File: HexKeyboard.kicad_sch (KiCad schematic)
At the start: 82 parts, among them J1 Conn_02x04_Odd_Even, J2 Conn_01x04, J4 USB_A, J9 Micro_SD_Card, SW1 SW_1, SW10 SW_10, SW11 SW_11, SW12 SW_12, SW13 SW_13, SW14 SW_14, SW15 SW_15, SW16 SW_16, SW17 SW_17, SW18 SW_18, SW19 SW_19, SW2 SW_2, SW20 SW_20, SW21 SW_21, SW22 SW_22, SW23 SW_23, SW24 SW_24, SW25 SW_25, SW3 SW_3, SW4 SW_4, SW5 SW_5, SW6 SW_6, SW7 SW_7, SW8 SW_8, SW9 SW_9, U1 ATmega32U4-AU, U2 AMS1117-3.3, U3 74LVC125, U4 AT24CS64-XHM, U5 MAX7219, Y1 16MHz

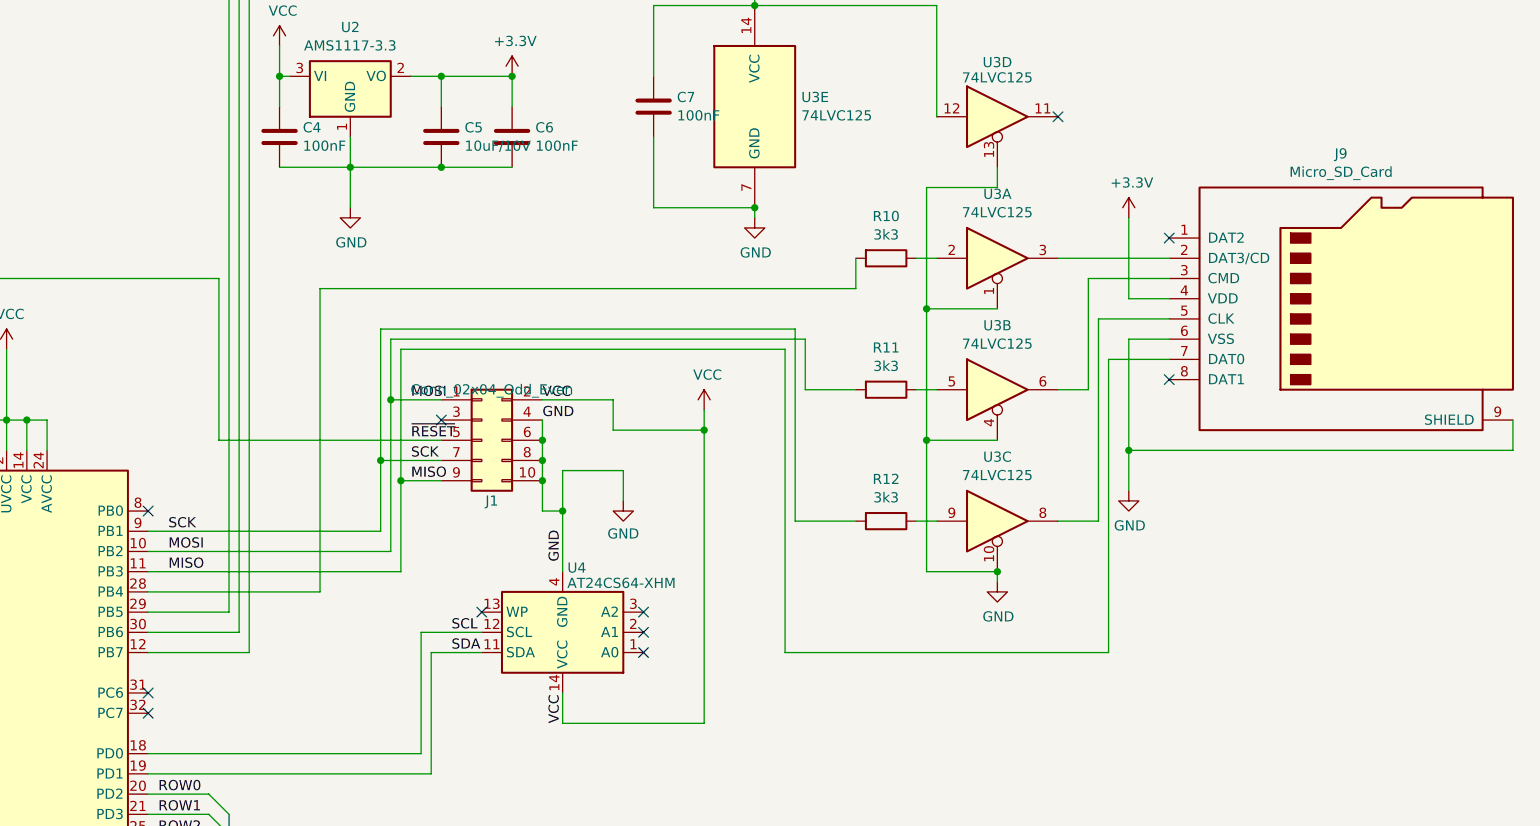
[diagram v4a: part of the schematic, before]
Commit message: Switched to the correct MicroSD holder
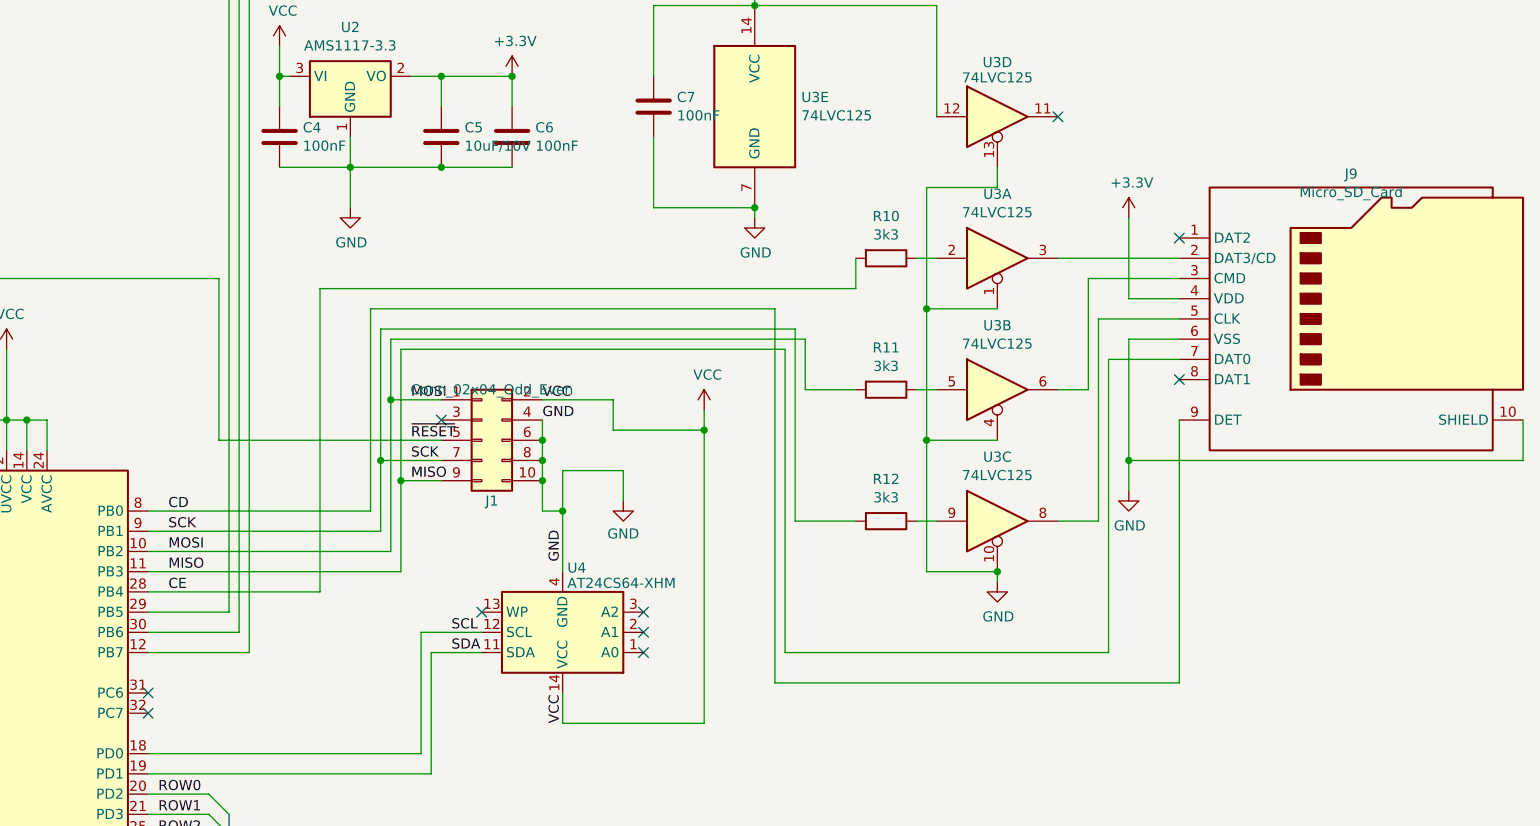
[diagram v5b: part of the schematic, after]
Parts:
- J9: footprint Connector_Card:microSD_HC_Wuerth_693072010801 -> MicroSD:GCT_MEM2075; symbol Connector:Micro_SD_Card -> Connector:Micro_SD_Card_Det1
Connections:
- net GND: now also J9.10 (SHIELD); no longer J9.9 (SHIELD)
- net CE: now reaches R10.2, U1.28 (PB4)
- net CD: now reaches U1.8 (PB0)
- net CD: now also J9.9 (DET)
- no-connect marks 18 -> 17
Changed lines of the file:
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@@
   (junction (at 96.52 83.82) (diameter 0) (color 0 0 0 0)
   )
-  (junction (at 312.42 151.13) (diameter 0) (color 0 0 0 0)
-  )
   (junction (at 171.45 147.32) (diameter 0) (color 0 0 0 0)
   )
@@
   )
   (junction (at 68.58 111.76) (diameter 0) (color 0 0 0 0)
+  )
+  (junction (at 312.42 152.4) (diameter 0) (color 0 0 0 0)
   )
   (junction (at 132.08 217.17) (diameter 0) (color 0 0 0 0)
@@
   (no_connect (at 251.46 176.53))
   (no_connect (at 251.46 171.45))
-  (no_connect (at 189.23 158.75))
-  (no_connect (at 317.5 124.46))
+  (no_connect (at 318.77 124.46))
   (no_connect (at 189.23 214.63))
   (no_connect (at 251.46 173.99))
@@
   (no_connect (at 226.06 147.32))
   (no_connect (at 189.23 207.01))
-  (no_connect (at 317.5 142.24))
+  (no_connect (at 318.77 142.24))
   (no_connect (at 231.14 171.45))
   (no_connect (at 189.23 212.09))
@@
     (stroke (width 0) (type default))
   )
-  (wire (pts (xy 308.61 134.62) (xy 317.5 134.62))
+  (wire (pts (xy 308.61 134.62) (xy 318.77 134.62))
     (stroke (width 0) (type default))
   )
@@
     (stroke (width 0) (type default))
   )
-  (wire (pts (xy 312.42 137.16) (xy 312.42 151.13))
-    (stroke (width 0) (type default))
-  )
   (wire (pts (xy 189.23 196.85) (xy 196.85 196.85))
     (stroke (width 0) (type default))
@@
     (stroke (width 0) (type default))
   )
+  (wire (pts (xy 312.42 152.4) (xy 312.42 156.21))
+    (stroke (width 0) (type default))
+  )
   (wire (pts (xy 252.73 104.14) (xy 252.73 95.25))
     (stroke (width 0) (type default))
@@
     (stroke (width 0) (type default))
   )
+  (wire (pts (xy 267.97 133.35) (xy 217.17 133.35))
+    (stroke (width 0) (type default))
+  )
   (wire (pts (xy 50.8 96.52) (xy 50.8 111.76))
     (stroke (width 0) (type default))
@@
     (stroke (width 0) (type default))
   )
+  (wire (pts (xy 267.97 180.34) (xy 267.97 133.35))
+    (stroke (width 0) (type default))
+  )
   (wire (pts (xy 214.63 111.76) (xy 214.63 115.57))
     (stroke (width 0) (type default))
@@
     (stroke (width 0) (type default))
   )
+  (wire (pts (xy 217.17 158.75) (xy 189.23 158.75))
+    (stroke (width 0) (type default))
+  )
   (wire (pts (xy 121.92 111.76) (xy 121.92 115.57))
     (stroke (width 0) (type default))
   )
-  (wire (pts (xy 307.34 129.54) (xy 317.5 129.54))
-    (stroke (width 0) (type default))
-  )
-  (wire (pts (xy 309.88 139.7) (xy 317.5 139.7))
+  (wire (pts (xy 307.34 129.54) (xy 318.77 129.54))
+    (stroke (width 0) (type default))
+  )
+  (wire (pts (xy 309.88 139.7) (xy 318.77 139.7))
     (stroke (width 0) (type default))
   )
@@
     (stroke (width 0) (type default))
   )
-  (wire (pts (xy 303.53 127) (xy 317.5 127))
-    (stroke (width 0) (type default))
-  )
   (bus (pts (xy 199.39 224.79) (xy 199.39 227.33))
     (stroke (width 0) (type default))
@@
     (stroke (width 0) (type default))
   )
-  (wire (pts (xy 360.68 147.32) (xy 360.68 151.13))
+  (wire (pts (xy 361.95 147.32) (xy 361.95 152.4))
     (stroke (width 0) (type default))
   )
@@
     (stroke (width 0) (type default))
   )
-  (wire (pts (xy 317.5 137.16) (xy 312.42 137.16))
+  (wire (pts (xy 318.77 137.16) (xy 312.42 137.16))
     (stroke (width 0) (type default))
   )
@@
     (stroke (width 0) (type default))
   )
-  (wire (pts (xy 312.42 151.13) (xy 312.42 156.21))
-    (stroke (width 0) (type default))
-  )
   (wire (pts (xy 100.33 234.95) (xy 116.84 234.95))
     (stroke (width 0) (type default))
@@
     (stroke (width 0) (type default))
   )
+  (wire (pts (xy 217.17 133.35) (xy 217.17 158.75))
+    (stroke (width 0) (type default))
+  )
   (wire (pts (xy 114.3 99.06) (xy 132.08 99.06))
     (stroke (width 0) (type default))
@@
     (stroke (width 0) (type default))
   )
+  (wire (pts (xy 312.42 137.16) (xy 312.42 152.4))
+    (stroke (width 0) (type default))
+  )
   (wire (pts (xy 223.52 189.23) (xy 223.52 173.99))
     (stroke (width 0) (type default))
@@
     (stroke (width 0) (type default))
   )
+  (wire (pts (xy 318.77 180.34) (xy 267.97 180.34))
+    (stroke (width 0) (type default))
+  )
   (bus (pts (xy 176.53 52.07) (xy 176.53 58.42))
     (stroke (width 0) (type default))
@@
     (stroke (width 0) (type default))
   )
-  (wire (pts (xy 317.5 132.08) (xy 312.42 132.08))
+  (wire (pts (xy 318.77 147.32) (xy 318.77 180.34))
+    (stroke (width 0) (type default))
+  )
+  (wire (pts (xy 318.77 132.08) (xy 312.42 132.08))
     (stroke (width 0) (type default))
   )
@@
     (stroke (width 0) (type default))
   )
-  (wire (pts (xy 360.68 151.13) (xy 312.42 151.13))
+  (wire (pts (xy 361.95 152.4) (xy 312.42 152.4))
     (stroke (width 0) (type default))
   )
@@
     (stroke (width 0) (type default))
   )
+  (wire (pts (xy 303.53 127) (xy 318.77 127))
+    (stroke (width 0) (type default))
+  )
   (wire (pts (xy 60.96 52.07) (xy 60.96 49.53))
     (stroke (width 0) (type default))
@@
     (effects (font (size 1.27 1.27)) (justify left bottom))
   )
+  (label "CD" (at 191.77 158.75 0) (fields_autoplaced)
+    (effects (font (size 1.27 1.27)) (justify left bottom))
+  )
   (label "VCC" (at 241.3 185.42 90) (fields_autoplaced)
     (effects (font (size 1.27 1.27)) (justify left bottom))
@@
   )
   (label "SCK" (at 191.77 161.29 0) (fields_autoplaced)
+    (effects (font (size 1.27 1.27)) (justify left bottom))
+  )
+  (label "CE" (at 191.77 168.91 0) (fields_autoplaced)
     (effects (font (size 1.27 1.27)) (justify left bottom))
   )
@@
     )
   )
-  (symbol (lib_id "Connector:Micro_SD_Card") (at 340.36 132.08 0) (unit 1)
-    (in_bom yes) (on_board yes) (dnp no)
-    (property "Reference" "J9" (at 339.09 113.8682 0)
-      (effects (font (size 1.27 1.27)))
-    )
-    (property "Value" "Micro_SD_Card" (at 339.09 116.1796 0)
-      (effects (font (size 1.27 1.27)))
-    )
-    (property "Footprint" "Connector_Card:microSD_HC_Wuerth_693072010801" (at 369.57 124.46 0)
-      (effects (font (size 1.27 1.27)) hide)
-    )
-    (property "Datasheet" "http://katalog.we-online.de/em/datasheet/693072010801.pdf" (at 340.36 132.08 0)
-      (effects (font (size 1.27 1.27)) hide)
-    )
-    (property "LCSC" "C5912397" (at 340.36 132.08 0)
-      (effects (font (size 1.27 1.27)) hide)
-    )
-    (pin "1")
+  (symbol (lib_id "Connector:Micro_SD_Card_Det1") (at 341.63 134.62 0) (unit 1)
+    (in_bom yes) (on_board yes) (dnp no)
+    (property "Reference" "J9" (at 340.36 116.4082 0)
+      (effects (font (size 1.27 1.27)))
+    )
+    (property "Value" "Micro_SD_Card" (at 340.36 118.7196 0)
+      (effects (font (size 1.27 1.27)))
+    )
+    (property "Footprint" "MicroSD:GCT_MEM2075" (at 393.7 116.84 0)
+      (effects (font (size 1.27 1.27)) hide)
+    )
+    (property "Datasheet" "https://datasheet.lcsc.com/lcsc/2110151630_XKB-Connectivity-XKTF-015-N_C381082.pdf" (at 341.63 132.08 0)
+      (effects (font (size 1.27 1.27)) hide)
+    )
+    (property "LCSC" "C5912397" (at 341.63 134.62 0)
+      (effects (font (size 1.27 1.27)) hide)
+    )
+    (pin "1")
+    (pin "10")
     (pin "2")
     (pin "3")

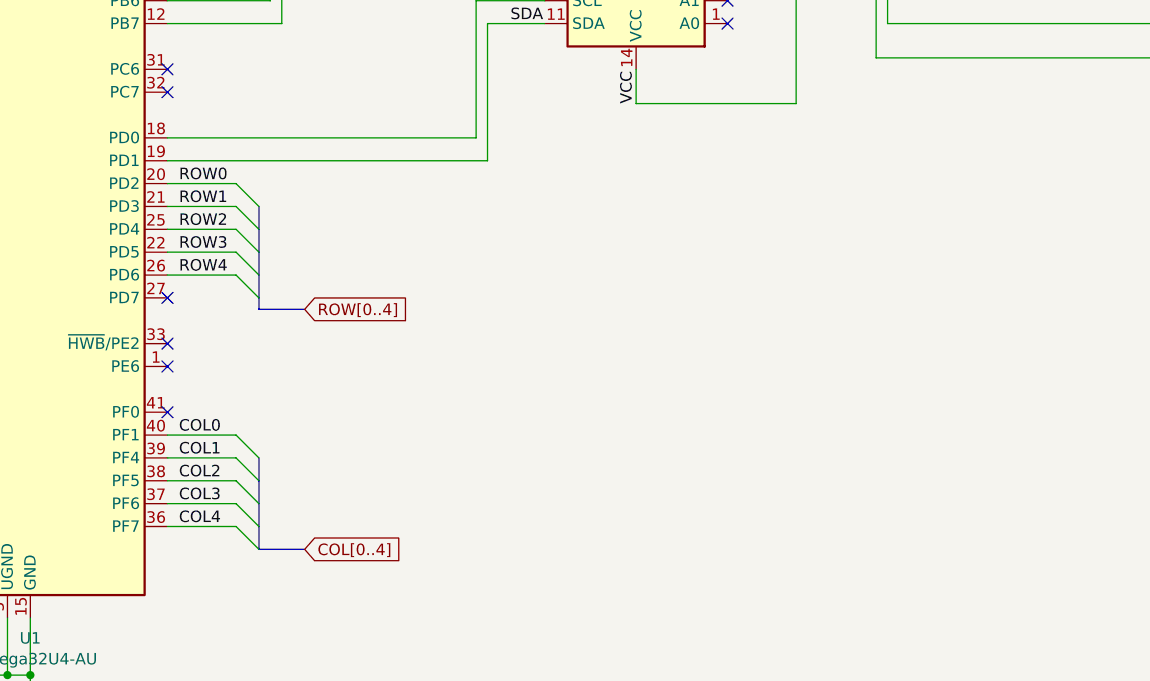
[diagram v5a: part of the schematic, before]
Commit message: Added serial port. Added new pin numbers to sketch
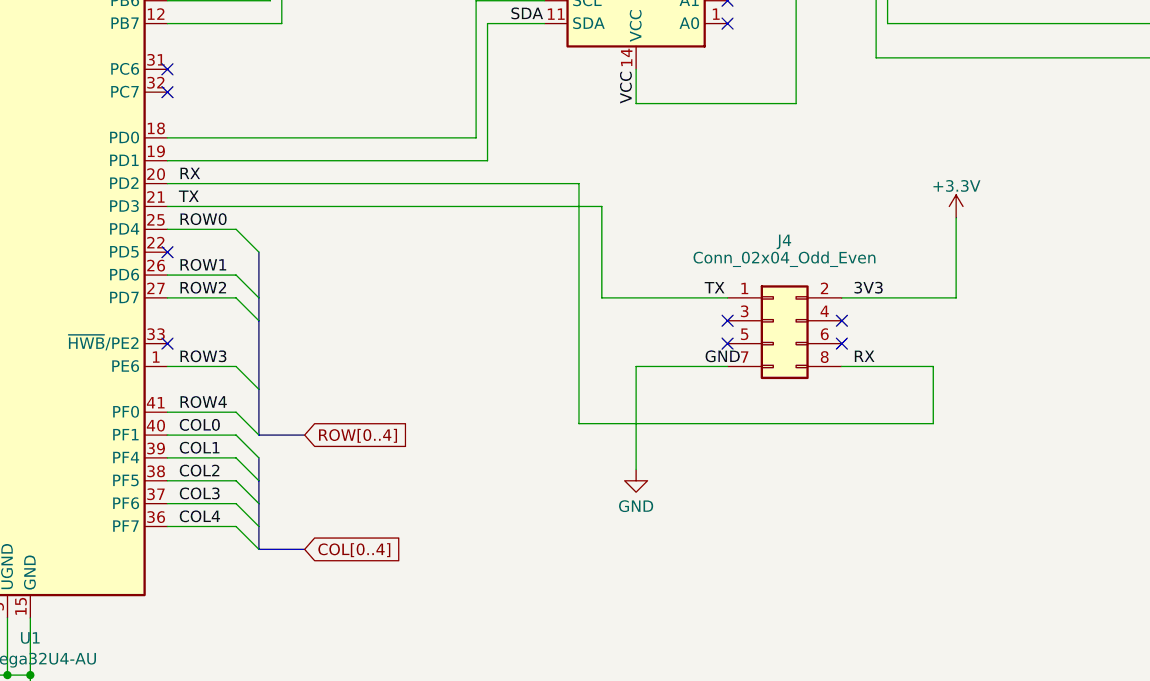
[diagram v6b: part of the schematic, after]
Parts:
- added J4: Conn_02x04_Odd_Even, Connector_PinHeader_2.54mm:PinHeader_2x04_P2.54mm_Vertical, symbol Connector_Generic:Conn_02x04_Odd_Even
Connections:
- net +3.3V: now also J4.2 (Pin_2)
- net GND: now also J4.7 (Pin_7)
- net ROW0: now also U1.25 (PD4); no longer U1.20 (PD2)
- net ROW1: now also U1.26 (PD6); no longer U1.21 (PD3)
- net ROW2: now also U1.27 (PD7); no longer U1.25 (PD4)
- net ROW3: now also U1.1 (PE6); no longer U1.22 (PD5)
- net ROW4: now also U1.41 (PF0); no longer U1.26 (PD6)
- new net RX: J4.8 (Pin_8), U1.20 (PD2)
- new net TX: J4.1 (Pin_1), U1.21 (PD3)
- no-connect marks 17 -> 19
